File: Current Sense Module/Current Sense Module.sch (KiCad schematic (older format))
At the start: 14 parts, among them J1 Conn_01x03_Male, J2 Conn_01x03_Male, J3 Conn_01x05_Male, U1 TLC2272

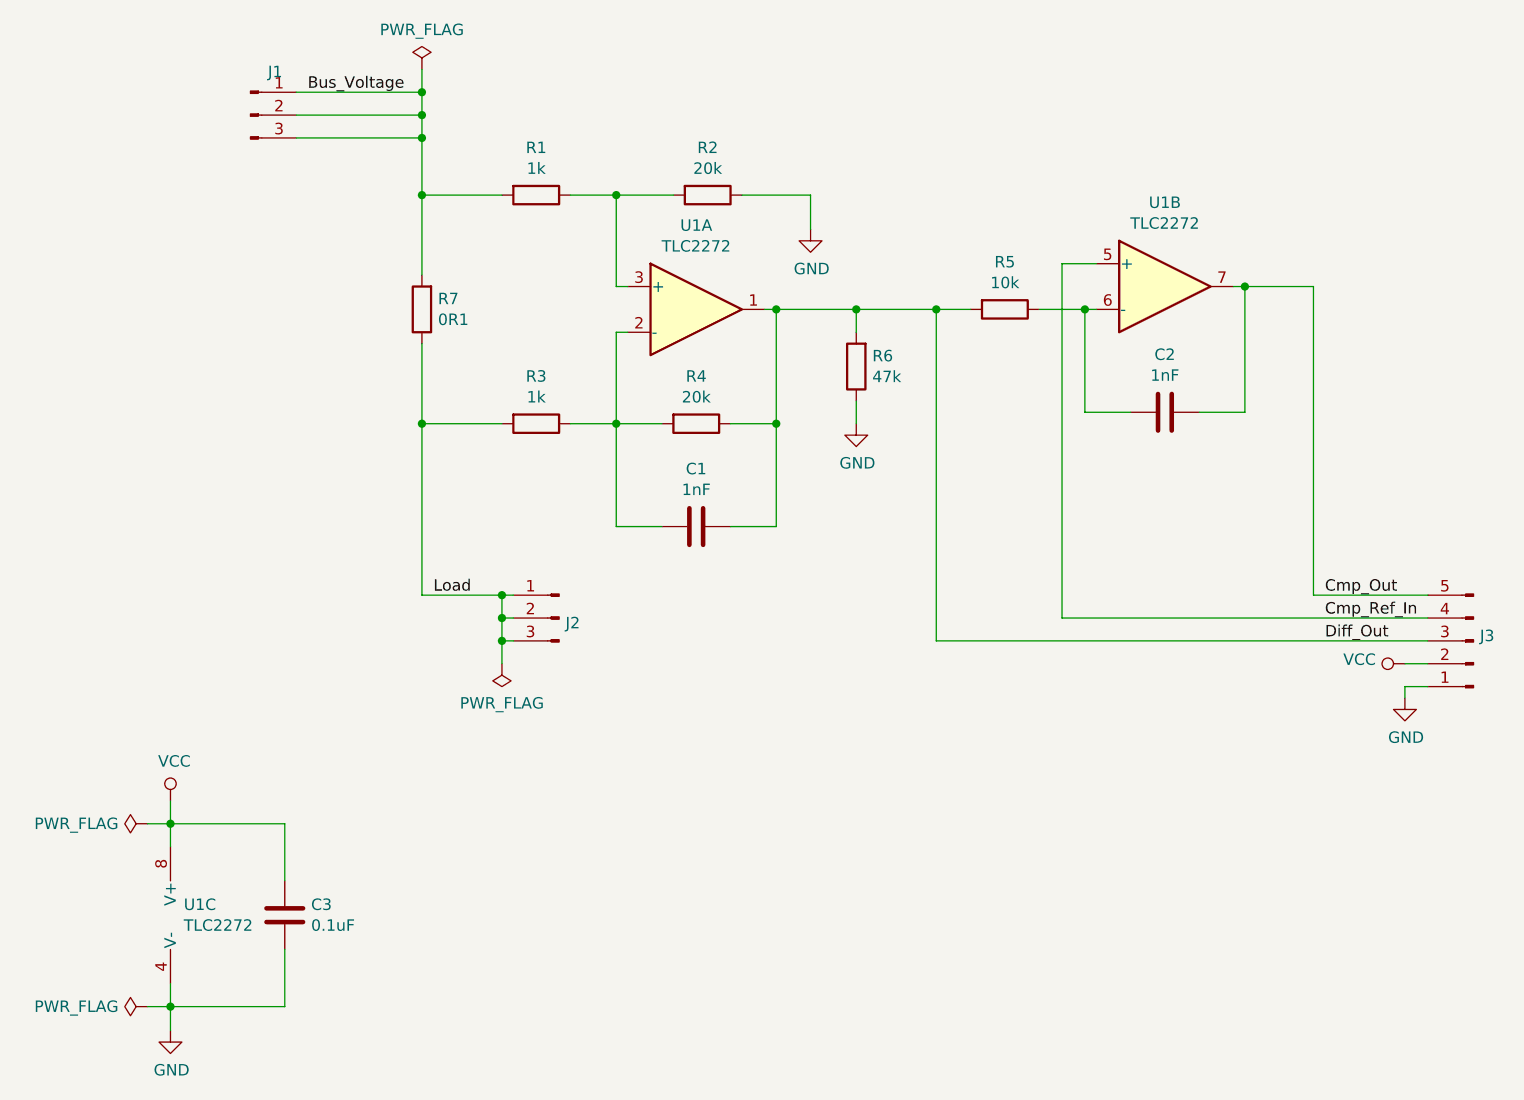
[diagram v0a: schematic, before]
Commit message: Completed PCB layout
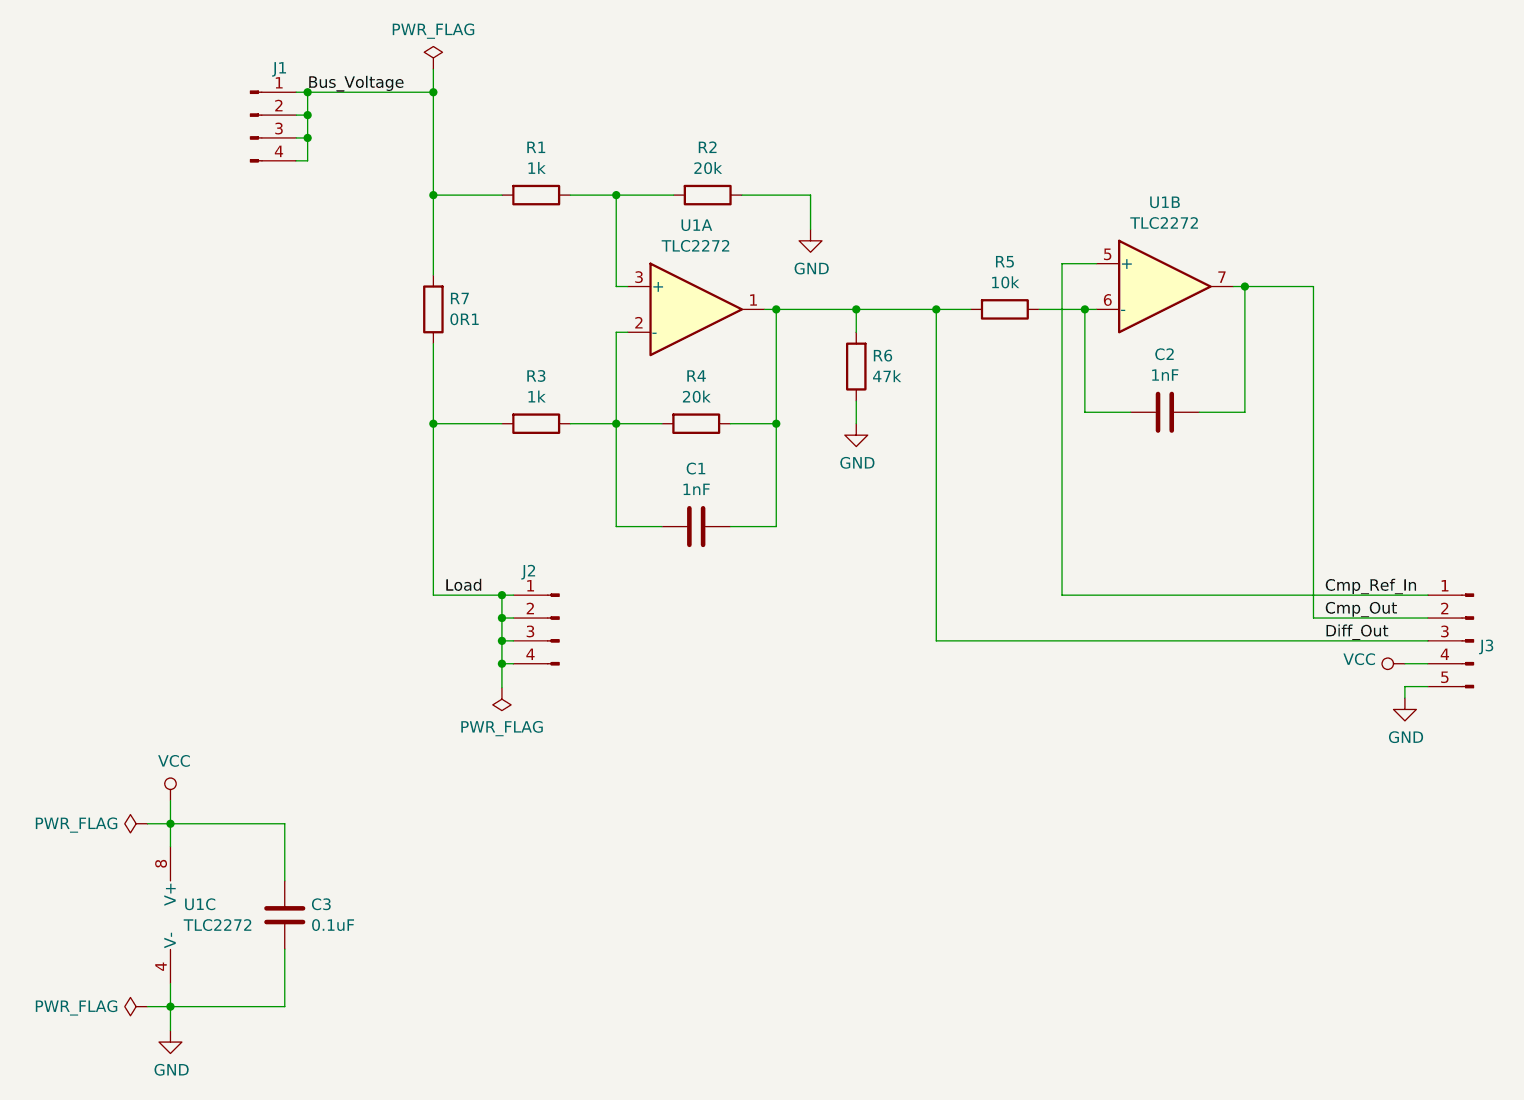
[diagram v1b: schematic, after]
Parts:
- removed J1, J2: Conn_01x03_Male, Pin_Headers:Pin_Header_Straight_1x03_Pitch2.54mm, symbol Connector:Conn_01x03_Male
- added J1, J2: Conn_01x04_Male, Pin_Headers:Pin_Header_Straight_2x02_Pitch2.54mm, symbol Connector:Conn_01x04_Male
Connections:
- net Bus_Voltage: now also J1.1 (Pin_1), J1.2 (Pin_2), J1.3 (Pin_3), J1.4 (Pin_4)
- net Cmp_Out: now also J3.2 (Pin_2); no longer J3.5 (Pin_5)
- net Cmp_Ref_In: now also J3.1 (Pin_1); no longer J3.4 (Pin_4)
- net GND: now also J3.5 (Pin_5); no longer J3.1 (Pin_1)
- net Load: now also J2.1 (Pin_1), J2.2 (Pin_2), J2.3 (Pin_3), J2.4 (Pin_4)
- net VCC: now also J3.4 (Pin_4); no longer J3.2 (Pin_2)
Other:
- moved on the sheet: R7
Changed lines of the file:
@@
 L Device:R R7
 U 1 1 601B083C
-P 4100 3250
-F 0 "R7" H 4030 3204 50  0000 R CNN
-F 1 "0R1" H 4030 3295 50  0000 R CNN
-F 2 "Current_Sense_Module:PCS2728DR1000ET" V 4030 3250 50  0001 C CNN
-F 3 "~" H 4100 3250 50  0001 C CNN
-	1    4100 3250
+P 4150 3250
+F 0 "R7" H 4080 3204 50  0000 R CNN
+F 1 "0R1" H 4080 3295 50  0000 R CNN
+F 2 "Current_Sense_Module:PCS2728DR1000ET" V 4080 3250 50  0001 C CNN
+F 3 "~" H 4150 3250 50  0001 C CNN
+	1    4150 3250
 	-1   0    0    1
 $EndComp
@@
 	5200 2750 4950 2750
 Wire Wire Line
-	4450 2750 4100 2750
-Wire Wire Line
-	4100 2750 4100 3100
-Wire Wire Line
-	4100 3400 4100 3750
-Wire Wire Line
-	4100 3750 4450 3750
+	4450 2750 4150 2750
+Wire Wire Line
+	4150 2750 4150 3100
+Wire Wire Line
+	4150 3400 4150 3750
+Wire Wire Line
+	4150 3750 4450 3750
 Wire Wire Line
 	4750 3750 4950 3750
@@
 Wire Wire Line
 	6800 3250 7000 3250
-$Comp
-L Connector:Conn_01x03_Male J2
-U 1 1 601E9591
-P 4700 4600
-F 0 "J2" H 4672 4578 50  0000 R CNN
-F 1 "Conn_01x03_Male" H 4672 4533 50  0001 R CNN
-F 2 "Pin_Headers:Pin_Header_Straight_1x03_Pitch2.54mm" H 4700 4600 50  0001 C CNN
-F 3 "~" H 4700 4600 50  0001 C CNN
-	1    4700 4600
-	-1   0    0    -1
-$EndComp
-Wire Wire Line
-	4100 2300 4100 2400
-Connection ~ 4100 2750
-Connection ~ 4100 2400
-Wire Wire Line
-	4100 2400 4100 2500
-Connection ~ 4100 2500
-Wire Wire Line
-	4100 2500 4100 2750
+Connection ~ 4150 2750
 Wire Wire Line
 	6500 3250 6350 3250
@@
 F 3 "~" H 8700 4700 50  0001 C CNN
 	1    8700 4700
-	-1   0    0    1
-$EndComp
-Wire Wire Line
-	8000 3150 8000 4500
-Wire Wire Line
-	8000 4500 8500 4500
-Wire Wire Line
-	6900 3050 6900 4600
-Wire Wire Line
-	6900 4600 8500 4600
+	-1   0    0    -1
+$EndComp
+Wire Wire Line
+	6900 3050 6900 4500
 Wire Wire Line
 	6900 3050 7050 3050
@@
 Wire Wire Line
 	8400 4900 8400 4950
+Text Label 8050 4600 0    50   ~ 0
+Cmp_Out
 Text Label 8050 4500 0    50   ~ 0
-Cmp_Out
-Text Label 8050 4600 0    50   ~ 0
 Cmp_Ref_In
 Text Label 8050 4700 0    50   ~ 0
 Diff_Out
 Wire Wire Line
-	4100 3750 4100 4500
-Connection ~ 4100 3750
-Wire Wire Line
-	4100 4500 4450 4500
+	4150 3750 4150 4500
+Connection ~ 4150 3750
+Wire Wire Line
+	4150 4500 4450 4500
 Wire Wire Line
 	4500 4600 4450 4600
@@
 	4450 4700 4450 4600
 Connection ~ 4450 4600
-Text Label 4150 4500 0    50   ~ 0
+Text Label 4200 4500 0    50   ~ 0
 Load
 Text Label 3600 2300 0    50   ~ 0
 Bus_Voltage
 Wire Wire Line
-	3550 2500 4100 2500
-Wire Wire Line
-	3550 2400 4100 2400
-Wire Wire Line
-	3550 2300 4100 2300
+	3550 2500 3600 2500
+Wire Wire Line
+	3550 2400 3600 2400
+Wire Wire Line
+	3550 2300 3600 2300
 $Comp
 L power:PWR_FLAG #FLG0101
 U 1 1 602813BF
-P 4100 2200
-F 0 "#FLG0101" H 4100 2275 50  0001 C CNN
-F 1 "PWR_FLAG" H 4100 2373 50  0000 C CNN
-F 2 "" H 4100 2200 50  0001 C CNN
-F 3 "~" H 4100 2200 50  0001 C CNN
-	1    4100 2200
-	1    0    0    -1
-$EndComp
-$Comp
-L Connector:Conn_01x03_Male J1
-U 1 1 60282F56
-P 3350 2400
-F 0 "J1" H 3458 2589 50  0000 C CNN
-F 1 "Conn_01x03_Male" H 3458 2590 50  0001 C CNN
-F 2 "Pin_Headers:Pin_Header_Straight_1x03_Pitch2.54mm" H 3350 2400 50  0001 C CNN
-F 3 "~" H 3350 2400 50  0001 C CNN
-	1    3350 2400
-	1    0    0    -1
-$EndComp
-Wire Wire Line
-	4100 2200 4100 2300
-Connection ~ 4100 2300
+P 4150 2200
+F 0 "#FLG0101" H 4150 2275 50  0001 C CNN
+F 1 "PWR_FLAG" H 4150 2373 50  0000 C CNN
+F 2 "" H 4150 2200 50  0001 C CNN
+F 3 "~" H 4150 2200 50  0001 C CNN
+	1    4150 2200
+	1    0    0    -1
+$EndComp
+Wire Wire Line
+	4150 2200 4150 2300
+Connection ~ 4150 2300
 $Comp
 L power:PWR_FLAG #FLG0102
 U 1 1 602899EC
-P 4450 4800
-F 0 "#FLG0102" H 4450 4875 50  0001 C CNN
-F 1 "PWR_FLAG" H 4450 4973 50  0000 C CNN
-F 2 "" H 4450 4800 50  0001 C CNN
-F 3 "~" H 4450 4800 50  0001 C CNN
-	1    4450 4800
+P 4450 4905
+F 0 "#FLG0102" H 4450 4980 50  0001 C CNN
+F 1 "PWR_FLAG" H 4450 5078 50  0000 C CNN
+F 2 "" H 4450 4905 50  0001 C CNN
+F 3 "~" H 4450 4905 50  0001 C CNN
+	1    4450 4905
 	-1   0    0    1
 $EndComp
 Wire Wire Line
-	4450 4800 4450 4700
+	4450 4905 4450 4800
 Connection ~ 4450 4700
 $Comp
@@
 Wire Wire Line
 	3000 6300 3005 6300
+$Comp
+L Connector:Conn_01x04_Male J1
+U 1 1 602B6F0F
+P 3350 2400
+F 0 "J1" H 3480 2605 50  0000 C CNN
+F 1 "Conn_01x04_Male" H 3458 2590 50  0001 C CNN
+F 2 "Pin_Headers:Pin_Header_Straight_2x02_Pitch2.54mm" H 3350 2400 50  0001 C CNN
+F 3 "~" H 3350 2400 50  0001 C CNN
+	1    3350 2400
+	1    0    0    -1
+$EndComp
+Wire Wire Line
+	3550 2600 3600 2600
+Wire Wire Line
+	3600 2600 3600 2500
+Connection ~ 3600 2500
+Wire Wire Line
+	3600 2500 3600 2400
+Connection ~ 3600 2400
+Wire Wire Line
+	3600 2400 3600 2300
+Connection ~ 3600 2300
+Wire Wire Line
+	3600 2300 4150 2300
+Wire Wire Line
+	4150 2300 4150 2750
+$Comp
+L Connector:Conn_01x04_Male J2
+U 1 1 602C6064
+P 4700 4600
+F 0 "J2" H 4830 4805 50  0000 C CNN
+F 1 "Conn_01x04_Male" H 4808 4790 50  0001 C CNN
+F 2 "Pin_Headers:Pin_Header_Straight_2x02_Pitch2.54mm" H 4700 4600 50  0001 C CNN
+F 3 "~" H 4700 4600 50  0001 C CNN
+	1    4700 4600
+	-1   0    0    -1
+$EndComp
+Wire Wire Line
+	4500 4800 4450 4800
+Connection ~ 4450 4800
+Wire Wire Line
+	4450 4800 4450 4700
+Wire Wire Line
+	8000 4600 8500 4600
+Wire Wire Line
+	8000 3150 8000 4600
+Wire Wire Line
+	6900 4500 8500 4500
 $EndSCHEMATC

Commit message: Schematic component update
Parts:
- C1: value 1nF -> 0p
- C2: value 1nF -> 330p
- C3: value 0.1uF -> 0.1u
- R1, R3: value 1k -> 1k 0.1%
- R2: value 20k -> 20k 0.1%
- R4: value 20k -> 20k 0.1 %
- R7: value 0R1 -> 0R1 0.5%
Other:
- note added: "Optional footprint."
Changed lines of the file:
@@
 EESchema Schematic File Version 4
+LIBS:Current Sense Module-cache
 EELAYER 29 0
 EELAYER END
@@
 P 4150 3250
 F 0 "R7" H 4080 3204 50  0000 R CNN
-F 1 "0R1" H 4080 3295 50  0000 R CNN
+F 1 "0R1 0.5%" H 4080 3295 50  0000 R CNN
 F 2 "Current_Sense_Module:PCS2728DR1000ET" V 4080 3250 50  0001 C CNN
 F 3 "~" H 4150 3250 50  0001 C CNN
@@
 P 5350 2750
 F 0 "R2" V 5143 2750 50  0000 C CNN
-F 1 "20k" V 5234 2750 50  0000 C CNN
+F 1 "20k 0.1%" V 5234 2750 50  0000 C CNN
 F 2 "Resistors_SMD:R_0805_HandSoldering" V 5280 2750 50  0001 C CNN
 F 3 "~" H 5350 2750 50  0001 C CNN
@@
 P 4600 3750
 F 0 "R3" V 4393 3750 50  0000 C CNN
-F 1 "1k" V 4484 3750 50  0000 C CNN
+F 1 "1k 0.1%" V 4484 3750 50  0000 C CNN
 F 2 "Resistors_SMD:R_0805_HandSoldering" V 4530 3750 50  0001 C CNN
 F 3 "~" H 4600 3750 50  0001 C CNN
@@
 P 5300 3750
 F 0 "R4" V 5093 3750 50  0000 C CNN
-F 1 "20k" V 5184 3750 50  0000 C CNN
+F 1 "20k 0.1 %" V 5184 3750 50  0000 C CNN
 F 2 "Resistors_SMD:R_0805_HandSoldering" V 5230 3750 50  0001 C CNN
 F 3 "~" H 5300 3750 50  0001 C CNN
@@
 P 4600 2750
 F 0 "R1" V 4393 2750 50  0000 C CNN
-F 1 "1k" V 4484 2750 50  0000 C CNN
+F 1 "1k 0.1%" V 4484 2750 50  0000 C CNN
 F 2 "Resistors_SMD:R_0805_HandSoldering" V 4530 2750 50  0001 C CNN
 F 3 "~" H 4600 2750 50  0001 C CNN
@@
 P 3500 5900
 F 0 "C3" H 3615 5946 50  0000 L CNN
-F 1 "0.1uF" H 3615 5855 50  0000 L CNN
+F 1 "0.1u" H 3615 5855 50  0000 L CNN
 F 2 "Capacitors_SMD:C_0805_HandSoldering" H 3538 5750 50  0001 C CNN
 F 3 "~" H 3500 5900 50  0001 C CNN
@@
 	3000 5400 3000 5500
 Wire Wire Line
-	3000 6200 3000 6300
-Wire Wire Line
 	3500 6050 3500 6300
-Connection ~ 3000 6300
-Wire Wire Line
-	3000 6300 3000 6405
 Wire Wire Line
 	3500 5750 3500 5500
@@
 P 5300 4200
 F 0 "C1" V 5048 4200 50  0000 C CNN
-F 1 "1nF" V 5139 4200 50  0000 C CNN
+F 1 "0p" V 5139 4200 50  0000 C CNN
 F 2 "Capacitors_SMD:C_0805_HandSoldering" H 5338 4050 50  0001 C CNN
 F 3 "~" H 5300 4200 50  0001 C CNN
@@
 P 7350 3700
 F 0 "C2" V 7098 3700 50  0000 C CNN
-F 1 "1nF" V 7189 3700 50  0000 C CNN
+F 1 "330p" V 7189 3700 50  0000 C CNN
 F 2 "Capacitors_SMD:C_0805_HandSoldering" H 7388 3550 50  0001 C CNN
 F 3 "~" H 7350 3700 50  0001 C CNN
@@
 Wire Wire Line
 	2900 5500 3000 5500
-Wire Wire Line
-	3500 6300 3000 6300
 $Comp
 L power:PWR_FLAG #FLG0104
@@
 	0    -1   -1   0
 $EndComp
-Wire Wire Line
-	2900 6300 3000 6300
-Wire Wire Line
-	3000 6300 3005 6300
 $Comp
 L Connector:Conn_01x04_Male J1
@@
 Wire Wire Line
 	6900 4500 8500 4500
+Text Notes 4960 4390 0    50   ~ 0
+Optional footprint.
+Wire Wire Line
+	3000 6300 3000 6405
+Wire Wire Line
+	3000 6200 3000 6300
+Wire Wire Line
+	3000 6300 3500 6300
+Wire Wire Line
+	2900 6300 3000 6300
+Connection ~ 3000 6300
 $EndSCHEMATC
